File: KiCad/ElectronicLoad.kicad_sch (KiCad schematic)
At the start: 158 parts, among them J1 LOAD, J4 12V, J5 USB, J6 PROG, M1 FAN, Q1 any, Q2 any, Q3 BSS138, SW1 FN, SW2 PROG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

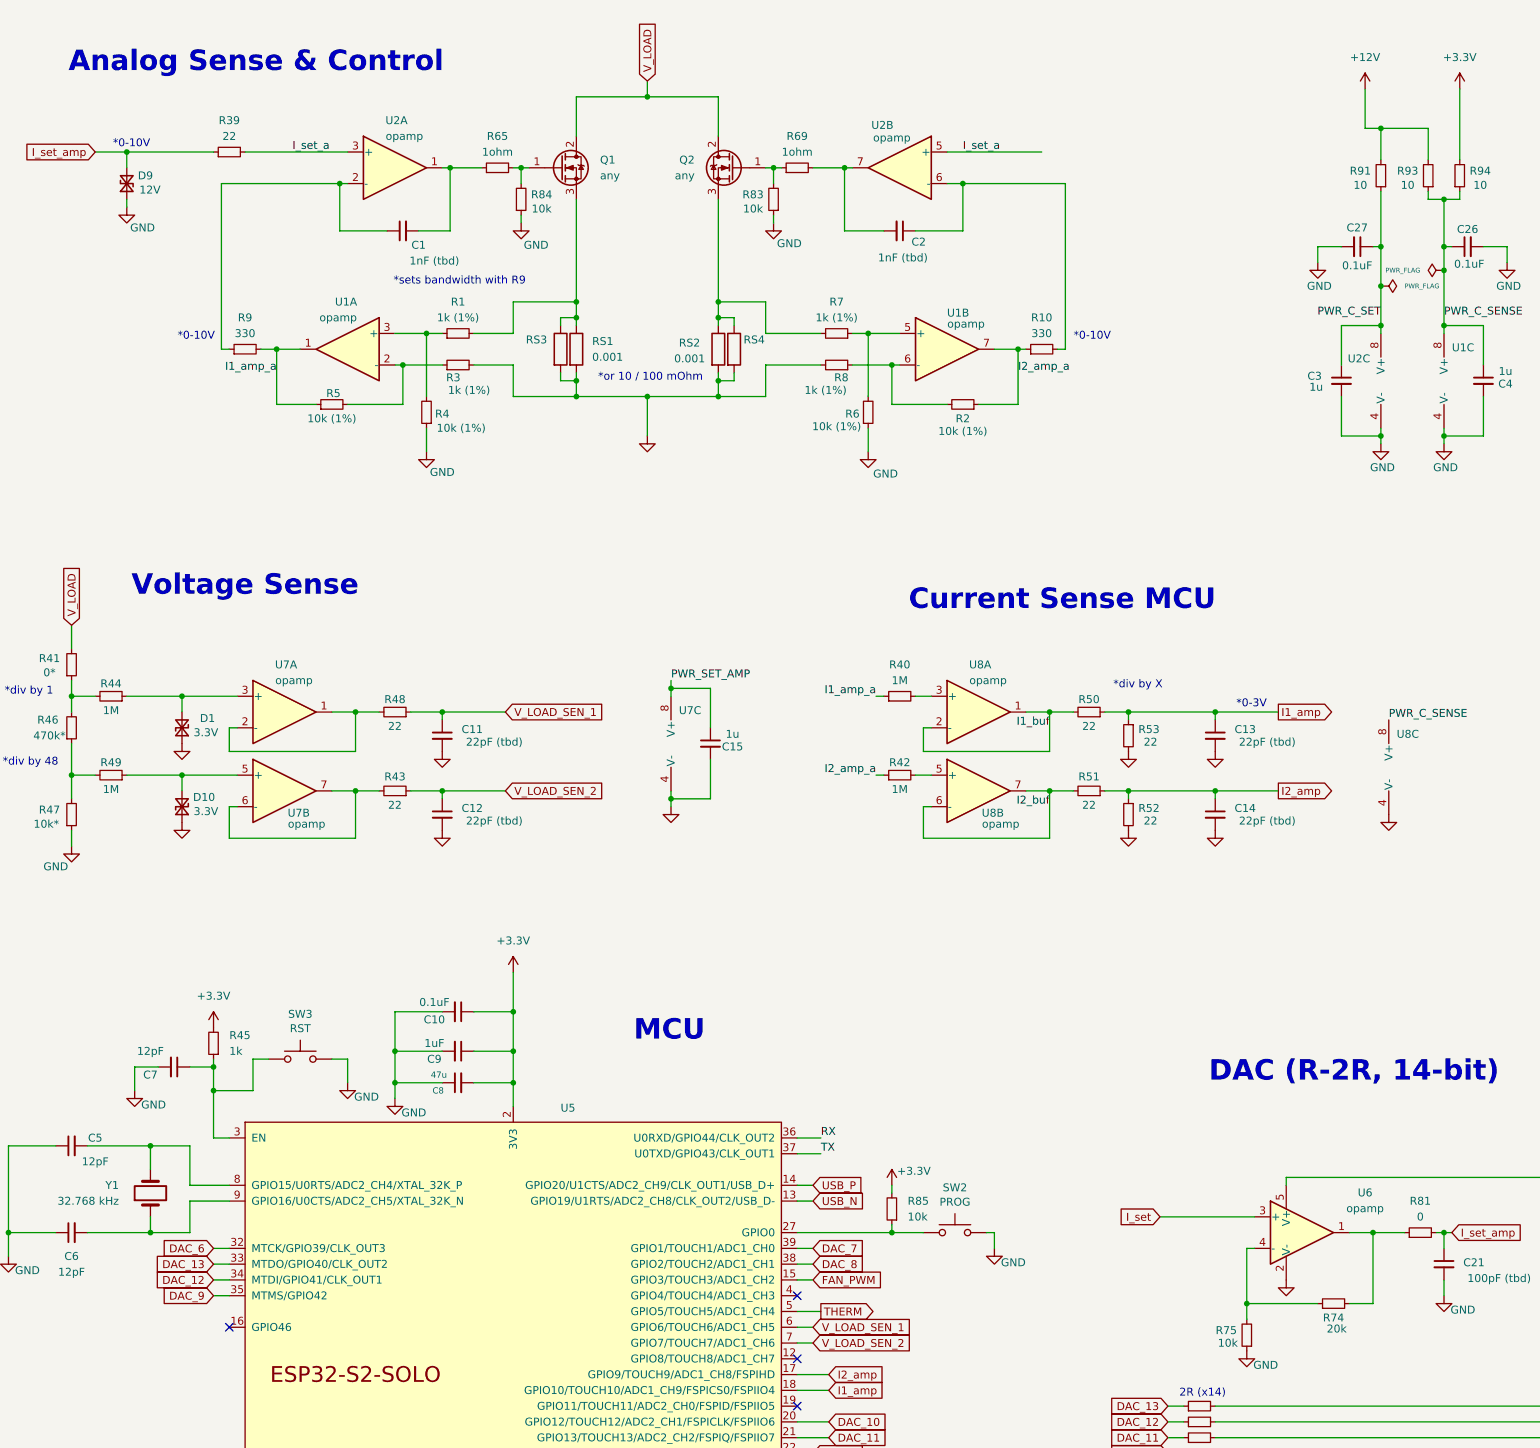
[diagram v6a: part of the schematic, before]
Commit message: rev0.2: add disable MOSFET-s signal
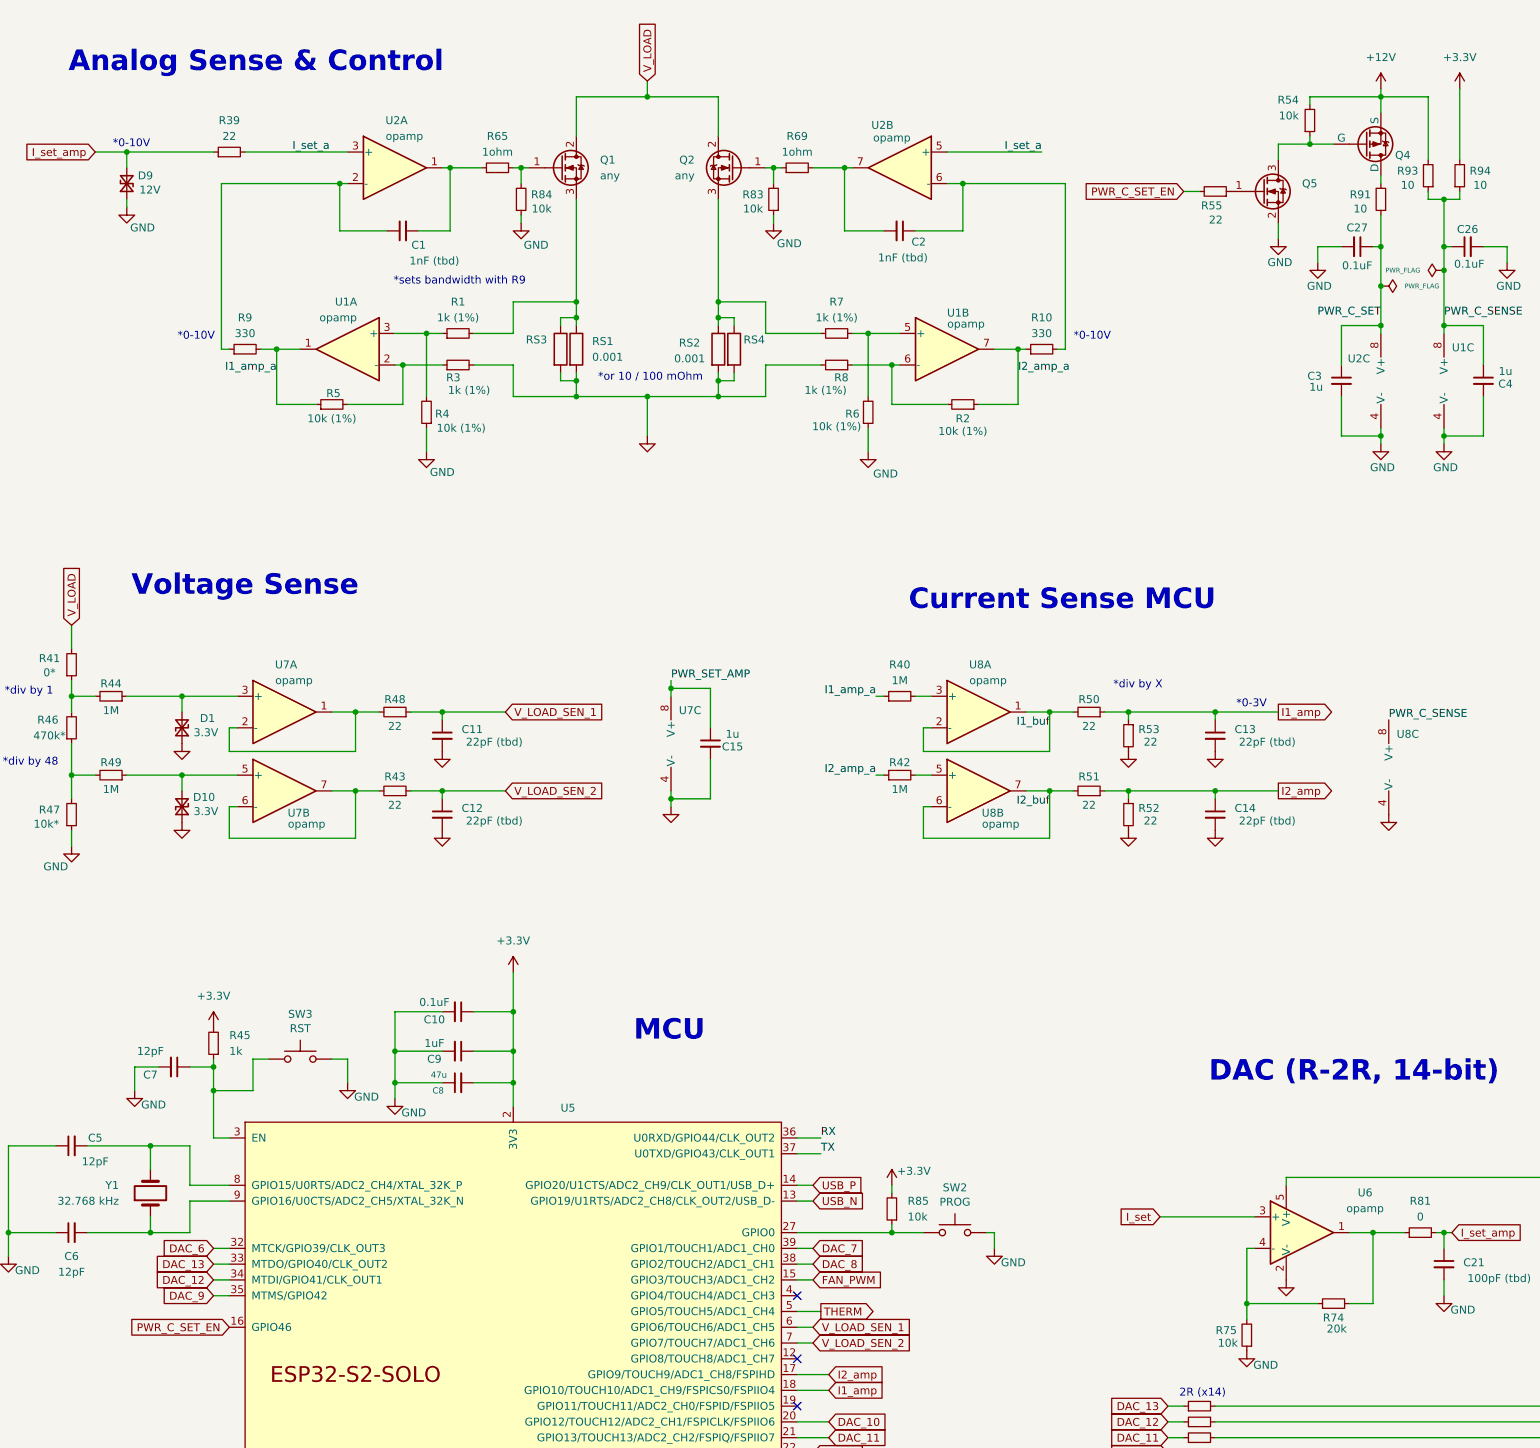
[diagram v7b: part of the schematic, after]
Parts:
- added Q4: PMOS, Package_TO_SOT_SMD:SOT-23, symbol Simulation_SPICE:PMOS
- added Q5: BSS138, Package_TO_SOT_SMD:SOT-23, symbol Transistor_FET:BSS138
- added R54: 10k, Resistor_SMD:R_0805_2012Metric, symbol Device:R_Small
- added R55: 22, Resistor_SMD:R_0805_2012Metric, symbol Device:R_Small
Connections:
- net +12V: now also Q4.3 (S), R54.2; no longer R91.2
- net GND: now also Q5.2 (S)
- net PWR_C_SET_EN: now reaches U5.16 (GPIO46)
- net PWR_C_SET_EN: now also R55.2
- new net: Q4.1 (D), R91.2
- new net: Q4.2 (G), Q5.3 (D), R54.1
- new net: Q5.1 (G), R55.1
- no-connect marks 10 -> 9
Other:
- moved on the sheet: R91

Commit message: rev0.2: adjust component values
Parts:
- C1, C2: value 1nF (tbd) -> 4.7nF
- C11, C12: value 22pF (tbd) -> 100pF
- C13, C14: value 22pF (tbd) -> 4.7nF
- C19: value 3.3pF (tbd) -> 100pF
- C21: value 100pF (tbd) -> 4.7nF
- D2: value D_Small -> Schottky
- R12, R13, R14, R15, R16, R17, R18, R19, R20, R201, R21, R22, R23, R24, R38: value R_Small -> 2k (1%)
- R25, R26, R27, R28, R29, R30, R31, R32, R33, R34, R35, R36, R37: value R_Small -> 1k (1%)
- R40, R42, R44, R49: value 1M -> 100k
- R41: value 0* -> 0
- R46: value 470k* -> 100k (1%)
- R47: value 10k* -> 10k (1%)
- R65, R69: value 1ohm -> 10
- R66: value 2.2k -> 3.3k
- R67: value 3.3k -> 10k
- R68: value 12k -> 22k
- R70: value R_Small -> 0
- R88, R89: value 1 -> 10
- R93: value 10 -> dnp
- R95: value 1ohm -> dnp
- R96: value dnp -> 1ohm
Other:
- note added: "1k (1%)"
- note added: "2k (1%)"
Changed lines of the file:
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@@
 		)
 	)
+	(text "2k (1%)"
+		(exclude_from_sim no)
+		(at 221.234 235.712 0)
+		(effects
+			(font
+				(size 1.27 1.27)
+			)
+		)
+	)
 	(text "*div by 48"
 		(exclude_from_sim no)
@@
 		)
 	)
+	(text "1k (1%)"
+		(exclude_from_sim no)
+		(at 256.032 263.144 0)
+		(effects
+			(font
+				(size 1.27 1.27)
+			)
+		)
+	)
 	(text "Current Sense MCU"
 		(exclude_from_sim no)
@@
 			)
 		)
-		(property "Value" "R_Small"
+		(property "Value" "2k (1%)"
 			(at 210.82 240.03 90)
 			(effects
@@
 			)
 		)
-		(property "Value" "R_Small"
+		(property "Value" "2k (1%)"
 			(at 210.82 257.81 90)
 			(effects
@@
 			)
 		)
-		(property "Value" "10k*"
-			(at 25.146 143.764 0)
+		(property "Value" "10k (1%)"
+			(at 23.368 143.764 0)
 			(effects
 				(font
@@
 			)
 		)
-		(property "Value" "R_Small"
+		(property "Value" "2k (1%)"
 			(at 210.82 234.95 90)
 			(effects
@@
 			)
 		)
-		(property "Value" "3.3pF (tbd)"
-			(at 289.814 245.618 0)
+		(property "Value" "100pF"
+			(at 287.782 245.11 0)
 			(effects
 				(font
@@
 			)
 		)
-		(property "Value" "R_Small"
+		(property "Value" "2k (1%)"
 			(at 210.82 252.73 90)
 			(effects
@@
 			)
 		)
-		(property "Value" "R_Small"
+		(property "Value" "2k (1%)"
 			(at 210.82 267.97 90)
 			(effects
@@
 			)
 		)
-		(property "Value" "R_Small"
+		(property "Value" "1k (1%)"
 			(at 218.44 270.51 90)
 			(effects
@@
 			)
 		)
-		(property "Value" "22pF (tbd)"
-			(at 97.282 130.556 0)
+		(property "Value" "100pF"
+			(at 94.488 130.556 0)
 			(effects
 				(font
@@
 			)
 		)
-		(property "Value" "R_Small"
+		(property "Value" "2k (1%)"
 			(at 210.82 276.86 90)
 			(effects
@@
 			)
 		)
-		(property "Value" "1"
+		(property "Value" "10"
 			(at 361.696 88.392 90)
 			(effects
@@
 			)
 		)
-		(property "Value" "D_Small"
+		(property "Value" "Schottky"
 			(at 370.84 67.31 0)
 			(effects
@@
 			)
 		)
-		(property "Value" "R_Small"
+		(property "Value" "2k (1%)"
 			(at 210.82 247.65 90)
 			(effects
@@
 			)
 		)
-		(property "Value" "22pF (tbd)"
-			(at 97.282 143.256 0)
+		(property "Value" "100pF"
+			(at 94.996 143.51 0)
 			(effects
 				(font
@@
 			)
 		)
-		(property "Value" "0*"
+		(property "Value" "0"
 			(at 25.654 119.38 0)
 			(effects
@@
 			)
 		)
-		(property "Value" "R_Small"
+		(property "Value" "2k (1%)"
 			(at 210.82 265.43 90)
 			(effects
@@
 			)
 		)
-		(property "Value" "R_Small"
+		(property "Value" "1k (1%)"
 			(at 259.08 250.19 90)
 			(effects
@@
 			)
 		)
-		(property "Value" "1M"
+		(property "Value" "100k"
 			(at 35.56 125.476 90)
 			(effects
@@
 			)
 		)
-		(property "Value" "R_Small"
+		(property "Value" "1k (1%)"
 			(at 264.16 247.65 90)
 			(effects
@@
 			)
 		)
-		(property "Value" "100pF (tbd)"
-			(at 259.08 216.916 0)
+		(property "Value" "4.7nF"
+			(at 255.778 216.916 0)
 			(effects
 				(font
@@
 			)
 		)
-		(property "Value" "R_Small"
+		(property "Value" "1k (1%)"
 			(at 233.68 262.89 90)
 			(effects
@@
 			)
 		)
-		(property "Value" "1nF (tbd)"
-			(at 87.63 53.086 90)
+		(property "Value" "4.7nF"
+			(at 85.598 52.832 90)
 			(effects
 				(font
@@
 			)
 		)
-		(property "Value" "22pF (tbd)"
-			(at 221.742 143.256 0)
+		(property "Value" "4.7nF"
+			(at 218.948 143.256 0)
 			(effects
 				(font
@@
 			)
 		)
-		(property "Value" "1ohm"
-			(at 275.082 194.564 0)
+		(property "Value" "dnp"
+			(at 275.844 194.564 0)
 			(effects
 				(font
@@
 			)
 		)
-		(property "Value" "R_Small"
+		(property "Value" "2k (1%)"
 			(at 210.82 255.27 90)
 			(effects
@@
 			)
 		)
-		(property "Value" "22pF (tbd)"
-			(at 221.742 130.556 0)
+		(property "Value" "4.7nF"
+			(at 218.948 130.556 0)
 			(effects
 				(font
@@
 			)
 		)
-		(property "Value" "10"
+		(property "Value" "dnp"
 			(at 244.348 40.894 0)
 			(effects
@@
 			)
 		)
-		(property "Value" "R_Small"
+		(property "Value" "1k (1%)"
 			(at 228.6 265.43 90)
 			(effects
@@
 			)
 		)
-		(property "Value" "12k"
+		(property "Value" "22k"
 			(at 325.628 98.044 0)
 			(effects
@@
 			)
 		)
-		(property "Value" "1M"
+		(property "Value" "100k"
 			(at 35.56 138.176 90)
 			(effects
@@
 			)
 		)
-		(property "Value" "dnp"
-			(at 287.782 194.564 0)
+		(property "Value" "1ohm"
+			(at 288.544 194.564 0)
 			(effects
 				(font
@@
 			)
 		)
-		(property "Value" "2.2k"
+		(property "Value" "3.3k"
 			(at 301.498 98.044 0)
 			(effects
@@
 			)
 		)
-		(property "Value" "R_Small"
+		(property "Value" "2k (1%)"
 			(at 210.82 242.57 90)
 			(effects
@@
 			)
 		)
-		(property "Value" "R_Small"
+		(property "Value" "1k (1%)"
 			(at 238.76 260.35 90)
 			(effects
@@
 			)
 		)
-		(property "Value" "3.3k"
+		(property "Value" "10k"
 			(at 314.198 98.044 0)
 			(effects
@@
 			)
 		)
-		(property "Value" "R_Small"
+		(property "Value" "1k (1%)"
 			(at 213.36 273.05 90)
 			(effects
@@
 			)
 		)
-		(property "Value" "R_Small"
+		(property "Value" "2k (1%)"
 			(at 210.82 262.89 90)
 			(effects
@@
 			)
 		)
-		(property "Value" "1ohm"
+		(property "Value" "10"
 			(at 146.05 35.56 90)
 			(effects
@@
 			)
 		)
-		(property "Value" "R_Small"
+		(property "Value" "1k (1%)"
 			(at 223.52 267.97 90)
 			(effects
@@
 			)
 		)
-		(property "Value" "R_Small"
+		(property "Value" "1k (1%)"
 			(at 254 252.73 90)
 			(effects
@@
 			)
 		)
-		(property "Value" "R_Small"
+		(property "Value" "1k (1%)"
 			(at 248.92 255.27 90)
 			(effects
@@
 			)
 		)
-		(property "Value" "R_Small"
+		(property "Value" "2k (1%)"
 			(at 210.82 237.49 90)
 			(effects
@@
 			)
 		)
-		(property "Value" "R_Small"
+		(property "Value" "1k (1%)"
 			(at 269.24 245.11 90)
 			(effects
@@
 			)
 		)
-		(property "Value" "1M"
+		(property "Value" "100k"
 			(at 162.56 138.176 90)
 			(effects
@@
 			)
 		)
-		(property "Value" "1nF (tbd)"
+		(property "Value" "4.7nF"
 			(at 163.068 52.578 90)
 			(effects
@@
 			)
 		)
-		(property "Value" "R_Small"
+		(property "Value" "1k (1%)"
 			(at 274.32 242.57 90)
 			(effects
@@
 			)
 		)
-		(property "Value" "R_Small"
+		(property "Value" "1k (1%)"
 			(at 243.84 257.81 90)
 			(effects
@@
 			)
 		)
-		(property "Value" "1"
+		(property "Value" "10"
 			(at 361.696 83.312 90)
 			(effects
@@
 		(dnp no)
 		(property "Reference" "R40"
-			(at 162.56 118.11 90)
+			(at 162.56 120.904 90)
 			(effects
 				(font
@@
 			)
 		)
-		(property "Value" "1M"
-			(at 162.56 120.65 90)
+		(property "Value" "100k"
+			(at 162.814 125.476 90)
 			(effects
 				(font
@@
 			)
 		)
-		(property "Value" "1ohm"
+		(property "Value" "10"
 			(at 97.79 35.56 90)
 			(effects
@@
 			)
 		)
-		(property "Value" "470k*"
-			(at 25.654 129.54 0)
+		(property "Value" "100k (1%)"
+			(at 22.86 129.54 0)
 			(effects
 				(font
@@
 			)
 		)
-		(property "Value" "R_Small"
+		(property "Value" "2k (1%)"
 			(at 210.82 250.19 90)
 			(effects
@@
 			)
 		)
-		(property "Value" "R_Small"
+		(property "Value" "2k (1%)"
 			(at 210.82 245.11 90)
 			(effects
@@
 			)
 		)
-		(property "Value" "R_Small"
+		(property "Value" "0"
 			(at 285.75 234.95 90)
 			(effects
@@
 					(size 1.27 1.27)
 				)
-				(hide yes)
 			)
 		)
@@
 			)
 		)
-		(property "Value" "R_Small"
+		(property "Value" "2k (1%)"
 			(at 210.82 260.35 90)
 			(effects
